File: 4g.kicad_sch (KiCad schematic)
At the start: 0 parts

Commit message: Adding 4G M.2 B
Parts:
- added J6: Bus_M.2_Socket_B, symbol Connector:Bus_M.2_Socket_B
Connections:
- new net +3.3V: J6.2 (3.3V), J6.4 (3.3V), J6.70 (3.3V), J6.72 (3.3V), J6.74 (3.3V)
- new net GND: J6.11 (GND), J6.21 (CONFIG_0), J6.27 (GND), J6.3 (GND), J6.33 (GND), J6.39 (GND), J6.45 (GND), J6.5 (GND), J6.51 (GND), J6.57 (GND), J6.69 (CONFIG_1), J6.71 (GND), J6.73 (GND), J6.75 (CONFIG_2), J6.8 (~{W_DISABLE1})
- new net USB0_D_N: J6.7 (USB_D+)
- new net USB0_D_P: J6.9 (USB_D-)
- no-connect marks 0 -> 3
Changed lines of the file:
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@@
 (kicad_sch (version 20230121) (generator eeschema)
   (paper "A4")
+  (junction (at 173.99 64.77) (diameter 0) (color 0 0 0 0)
+  )
+  (junction (at 173.99 62.23) (diameter 0) (color 0 0 0 0)
+  )
+  (no_connect (at 168.91 67.31))
+  (no_connect (at 118.11 133.35))
+  (no_connect (at 168.91 86.995))
+  (wire (pts (xy 168.91 59.69) (xy 173.99 59.69))
+    (stroke (width 0) (type default))
+  )
+  (wire (pts (xy 143.51 151.13) (xy 143.51 153.67))
+    (stroke (width 0) (type default))
+  )
+  (wire (pts (xy 115.57 95.25) (xy 118.11 95.25))
+    (stroke (width 0) (type default))
+  )
+  (wire (pts (xy 168.91 84.455) (xy 171.45 84.455))
+    (stroke (width 0) (type default))
+  )
+  (wire (pts (xy 168.91 64.77) (xy 173.99 64.77))
+    (stroke (width 0) (type default))
+  )
+  (wire (pts (xy 168.91 62.23) (xy 173.99 62.23))
+    (stroke (width 0) (type default))
+  )
+  (wire (pts (xy 173.99 62.23) (xy 173.99 64.77))
+    (stroke (width 0) (type default))
+  )
+  (wire (pts (xy 173.99 59.69) (xy 173.99 62.23))
+    (stroke (width 0) (type default))
+  )
+  (wire (pts (xy 115.57 92.71) (xy 118.11 92.71))
+    (stroke (width 0) (type default))
+  )
+  (wire (pts (xy 143.51 52.07) (xy 143.51 54.61))
+    (stroke (width 0) (type default))
+  )
+  (global_label "USB0_D_N" (shape input) (at 115.57 92.71 180)
+    (effects (font (size 1.27 1.27)) (justify right))
+    (property "Intersheetrefs" "${INTERSHEET_REFS}" (at 99.695 92.71 0)
+      (effects (font (size 1.1 1.1)) (justify right))
+    )
+  )
+  (global_label "USB0_D_P" (shape input) (at 115.57 95.25 180)
+    (effects (font (size 1.27 1.27)) (justify right))
+    (property "Intersheetrefs" "${INTERSHEET_REFS}" (at 99.695 95.25 0)
+      (effects (font (size 1.1 1.1)) (justify right))
+    )
+  )
+  (symbol (lib_id "power:+3.3V") (at 143.51 52.07 0) (unit 1)
+    (in_bom yes) (on_board yes) (dnp no) (fields_autoplaced)
+    (property "Reference" "#PWR031" (at 143.51 55.88 0)
+      (effects (font (size 1.27 1.27)) hide)
+    )
+    (property "Value" "+3.3V" (at 143.51 46.99 0)
+      (effects (font (size 1.27 1.27)))
+    )
+    (property "Footprint" "" (at 143.51 52.07 0)
+      (effects (font (size 1.27 1.27)) hide)
+    )
+    (property "Datasheet" "" (at 143.51 52.07 0)
+      (effects (font (size 1.27 1.27)) hide)
+    )
+    (pin "1")
+    (instances
+      (project "jetson-orin-baseboard"
+        (path "/4b393452-b11e-416e-bc83-918ae3cab2f1/2fa436cd-5c26-4e4a-b48c-59983497db7a"
+          (reference "#PWR031") (unit 1)
+        )
+      )
+    )
+  )
+  (symbol (lib_id "power:GND") (at 171.45 84.455 0) (unit 1)
+    (in_bom yes) (on_board yes) (dnp no) (fields_autoplaced)
+    (property "Reference" "#PWR032" (at 171.45 90.805 0)
+      (effects (font (size 1.27 1.27)) hide)
+    )
+    (property "Value" "GND" (at 171.45 88.9 0)
+      (effects (font (size 1.27 1.27)))
+    )
+    (property "Footprint" "" (at 171.45 84.455 0)
+      (effects (font (size 1.27 1.27)) hide)
+    )
+    (property "Datasheet" "" (at 171.45 84.455 0)
+      (effects (font (size 1.27 1.27)) hide)
+    )
+    (pin "1")
+    (instances
+      (project "jetson-orin-baseboard"
+        (path "/4b393452-b11e-416e-bc83-918ae3cab2f1/2fa436cd-5c26-4e4a-b48c-59983497db7a"
+          (reference "#PWR032") (unit 1)
+        )
+      )
+    )
+  )
+  (symbol (lib_id "power:GND") (at 173.99 64.77 0) (unit 1)
+    (in_bom yes) (on_board yes) (dnp no) (fields_autoplaced)
+    (property "Reference" "#PWR030" (at 173.99 71.12 0)
+      (effects (font (size 1.27 1.27)) hide)
+    )
+    (property "Value" "GND" (at 173.99 69.85 0)
+      (effects (font (size 1.27 1.27)))
+    )
+    (property "Footprint" "" (at 173.99 64.77 0)
+      (effects (font (size 1.27 1.27)) hide)
+    )
+    (property "Datasheet" "" (at 173.99 64.77 0)
+      (effects (font (size 1.27 1.27)) hide)
+    )
+    (pin "1")
+    (instances
+      (project "jetson-orin-baseboard"
+        (path "/4b393452-b11e-416e-bc83-918ae3cab2f1/2fa436cd-5c26-4e4a-b48c-59983497db7a"
+          (reference "#PWR030") (unit 1)
+        )
+      )
+    )
+  )
+  (symbol (lib_id "power:GND") (at 143.51 153.67 0) (unit 1)
+    (in_bom yes) (on_board yes) (dnp no) (fields_autoplaced)
+    (property "Reference" "#PWR029" (at 143.51 160.02 0)
+      (effects (font (size 1.27 1.27)) hide)
+    )
+    (property "Value" "GND" (at 143.51 158.75 0)
+      (effects (font (size 1.27 1.27)))
+    )
+    (property "Footprint" "" (at 143.51 153.67 0)
+      (effects (font (size 1.27 1.27)) hide)
+    )
+    (property "Datasheet" "" (at 143.51 153.67 0)
+      (effects (font (size 1.27 1.27)) hide)
+    )
+    (pin "1")
+    (instances
+      (project "jetson-orin-baseboard"
+        (path "/4b393452-b11e-416e-bc83-918ae3cab2f1/2fa436cd-5c26-4e4a-b48c-59983497db7a"
+          (reference "#PWR029") (unit 1)
+        )
+      )
+    )
+  )
+  (symbol (lib_id "Connector:Bus_M.2_Socket_B") (at 143.51 102.87 0) (unit 1)
+    (in_bom yes) (on_board yes) (dnp no) (fields_autoplaced)
+    (property "Reference" "J6" (at 145.7041 51.689 0)
+      (effects (font (size 1.27 1.27)) (justify left))
+    )
+    (property "Value" "Bus_M.2_Socket_B" (at 145.7041 54.229 0)
+      (effects (font (size 1.27 1.27)) (justify left))
+    )
+    (property "Footprint" "" (at 143.51 76.2 0)
+      (effects (font (size 1.27 1.27)) hide)
+    )
+    (property "Datasheet" "https://www.waveshare.com/w/upload/0/02/SIM7600X-M2_Hardware_Design_V1.01.pdf" (at 143.51 76.2 0)
+      (effects (font (size 1.27 1.27)) hide)
+    )
+    (pin "1")
+    (pin "10")
+    (pin "11")
+    (pin "2")
+    (pin "20")
+    (pin "21")
+    (pin "22")
+    (pin "23")
+    (pin "24")
+    (pin "25")
+    (pin "26")
+    (pin "27")
+    (pin "28")
+    (pin "29")
+    (pin "3")
+    (pin "30")
+    (pin "31")
+    (pin "32")
+    (pin "33")
+    (pin "34")
+    (pin "35")
+    (pin "36")
+    (pin "37")
+    (pin "38")
+    (pin "39")
+    (pin "4")
+    (pin "40")
+    (pin "41")
+    (pin "42")
+    (pin "43")
+    (pin "44")
+    (pin "45")
+    (pin "46")
+    (pin "47")
+    (pin "48")
+    (pin "49")
+    (pin "5")
+    (pin "50")
+    (pin "51")
+    (pin "52")
+    (pin "53")
+    (pin "54")
+    (pin "55")
+    (pin "56")
+    (pin "57")
+    (pin "58")
+    (pin "59")
+    (pin "6")
+    (pin "60")
+    (pin "61")
+    (pin "62")
+    (pin "63")
+    (pin "64")
+    (pin "65")
+    (pin "66")
+    (pin "67")
+    (pin "68")
+    (pin "69")
+    (pin "7")
+    (pin "70")
+    (pin "71")
+    (pin "72")
+    (pin "73")
+    (pin "74")
+    (pin "75")
+    (pin "8")
+    (pin "9")
+    (instances
+      (project "jetson-orin-baseboard"
+        (path "/4b393452-b11e-416e-bc83-918ae3cab2f1/2fa436cd-5c26-4e4a-b48c-59983497db7a"
+          (reference "J6") (unit 1)
+        )
+      )
+    )
+  )
 )

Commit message: 4G V1 Done
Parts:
- removed J6: Bus_M.2_Socket_B, symbol Connector:Bus_M.2_Socket_B
- added C35: 100n, symbol Device:C
- added C45, C53, C64: 22p, symbol Device:C
- added D26: LTST-C190GKT, jetson-orin-baseboard-footprints:LED_0603, symbol jetson-orin-baseboard:LTST-C190GKT
- added D50 (x2): TPD1E0B04DPYR, jetson-orin-baseboard-footprints:XDFN-2_1x0.60mm, symbol jetson-orin-baseboard:TPD1E0B04DPYR
- added D8: ESDA6V1-5SC6, Package_TO_SOT_SMD:SOT-23-6, symbol Power_Protection:ESDA6V1-5SC6
- added J3: SIM7600X-M2-B, symbol jetson-orin-baseboard:SIM7600X-M2-B
- added J6: SIM8066-6-1-14-01-A, symbol jetson-orin-baseboard:SIM_Card_With_Detect
- added R223: R_200R_0402, jetson-orin-baseboard-footprints:0402-res, symbol jetson-orin-baseboard:R_200R_0402
- added R27, R28, R30: 22, symbol Device:R
- added R29, R31, R32, R34: 0, symbol Device:R
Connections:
- net +3.3V: now also J3.2 (3.3V), J3.4 (3.3V), J3.70 (3.3V), J3.72 (3.3V), J3.74 (3.3V)
- net GND: now also C35.2, C45.2, C53.2, C64.2, D50.1, D50.1, D8.2 (GND), J3.11 (GND), J3.21 (CONFIG_0), J3.27 (GND), J3.3 (GND), J3.33 (GND), J3.39 (GND), J3.45 (GND), J3.5 (GND), J3.51 (GND), J3.57 (GND), J3.69 (CONFIG_1), J3.71 (GND), J3.73 (GND), J3.75 (CONFIG_2), J6.5 (GND)
- net USB0_D_N: now also D50.2, R31.1
- net USB0_D_P: now also D50.2, R32.1
- new net: D26.2, J3.10 (~{LED1})
- new net: C64.1, D8.1 (IO1), J3.30 (USIM-RST), R30.2
- new net: C53.1, D8.3 (IO2), J3.32 (USIM-CLK), R29.2
- new net: C45.1, D8.4 (IO3), J3.34 (USIM-DATA), R28.2
- new net: D8.5 (IO4), J3.36 (USIM_VDD), J6.1 (VCC)
- new net: J3.6 (~{FULL_CARD_POWER_OFF}), R34.2
- new net: D8.6 (IO5), J3.66 (USIM_DET), R27.2
- new net: J3.7 (USB_D+), R31.2
- new net: J3.9 (USB_D-), R32.2
- new net: J6.7 (I/O), R28.1
- new net: D26.1, R223.1
- new net: J6.3 (CLK), R29.1
- new net: J6.4 (CD), R27.1
- new net: J6.2 (RST), R30.1
- new net +3V3: R223.2, R34.1
- no-connect marks 3 -> 28
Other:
- note added: "4G"

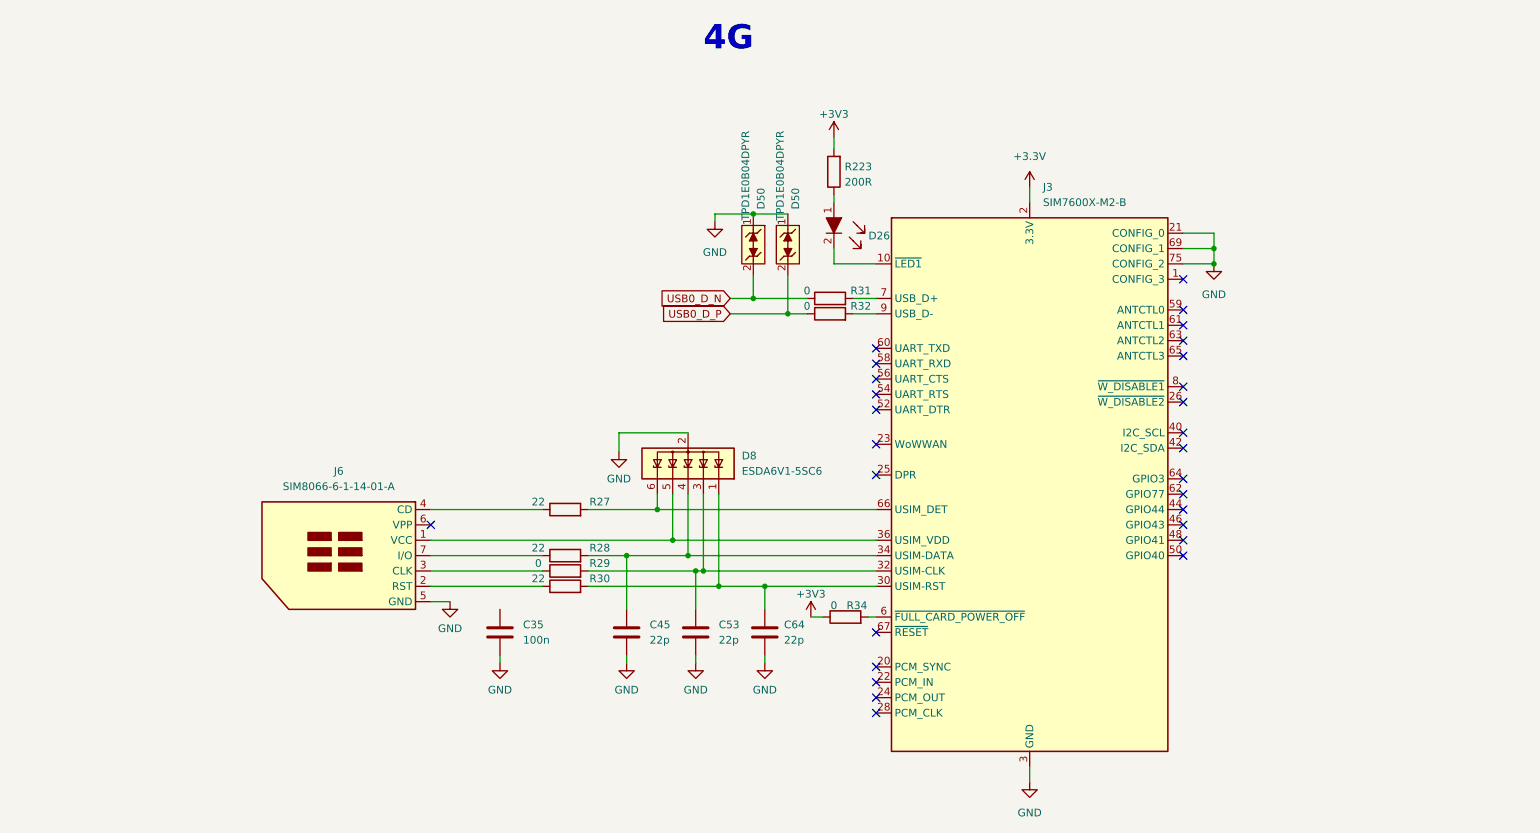
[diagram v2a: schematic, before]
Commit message: Schematic check
Include Pinmux and Schematic Check excels in doc folder and doing a lot of checking and correcting things.
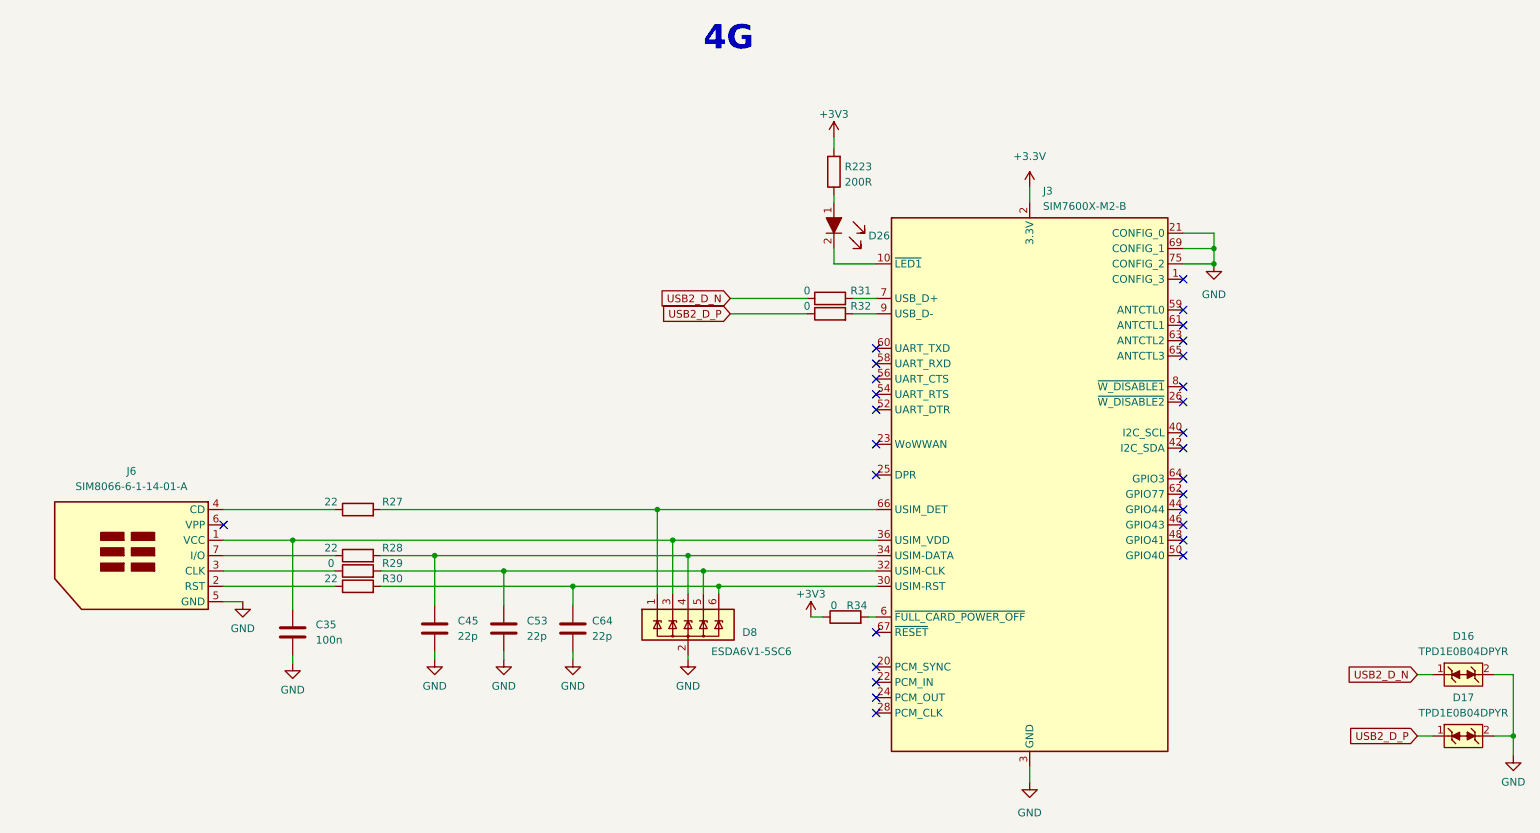
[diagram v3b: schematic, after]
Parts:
- removed D50 (x2): TPD1E0B04DPYR, jetson-orin-baseboard-footprints:XDFN-2_1x0.60mm, symbol jetson-orin-baseboard:TPD1E0B04DPYR
- added D16, D17: TPD1E0B04DPYR, jetson-orin-baseboard-footprints:XDFN-2_1x0.60mm, symbol jetson-orin-baseboard:TPD1E0B04DPYR
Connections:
- net GND: now also D16.2, D17.2
- net at C64.1, J3.30 (USIM-RST), R30.2: now also D8.6 (IO5); no longer D8.1 (IO1)
- net at C53.1, J3.32 (USIM-CLK), R29.2: now also D8.5 (IO4); no longer D8.3 (IO2)
- net at J3.36 (USIM_VDD), J6.1 (VCC): now also C35.1, D8.3 (IO2); no longer D8.5 (IO4)
- net at J3.66 (USIM_DET), R27.2: now also D8.1 (IO1); no longer D8.6 (IO5)
- net USB0_D_N renamed USB2_D_N
- net USB2_D_N: now also D16.1
- net USB0_D_P renamed USB2_D_P
- net USB2_D_P: now also D17.1
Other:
- moved on the sheet: C35, C45, C53, C64, D8, J6, R27, R28, R29, R30
